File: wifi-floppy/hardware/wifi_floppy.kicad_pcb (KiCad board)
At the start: 2 copper layers, 61.4 x 54 mm, 30 parts, among them J1 Conn_02x17_Odd_Even, J2 Conn_01x04, J3 Conn_01x04, J4 Conn_01x04, Q1 BSS138, Q2 BSS138, Q3 BSS138, Q4 BSS138, Q5 BSS138, Q6 BSS138, Q7 BSS138, Q8 BSS138, U1 RaspberryPi_Pico_W, U2 74LVC541A

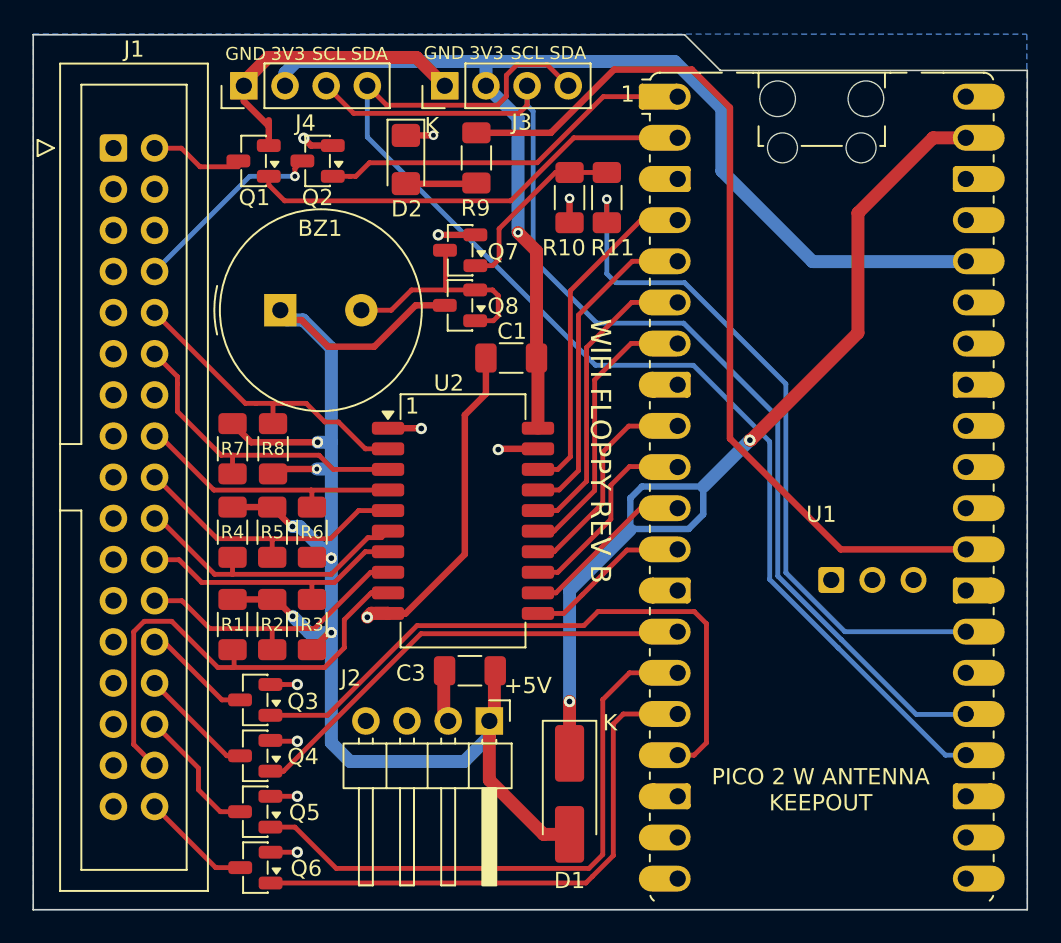
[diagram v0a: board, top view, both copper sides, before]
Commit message: Add the 22 ohms resistor for the buzzer.
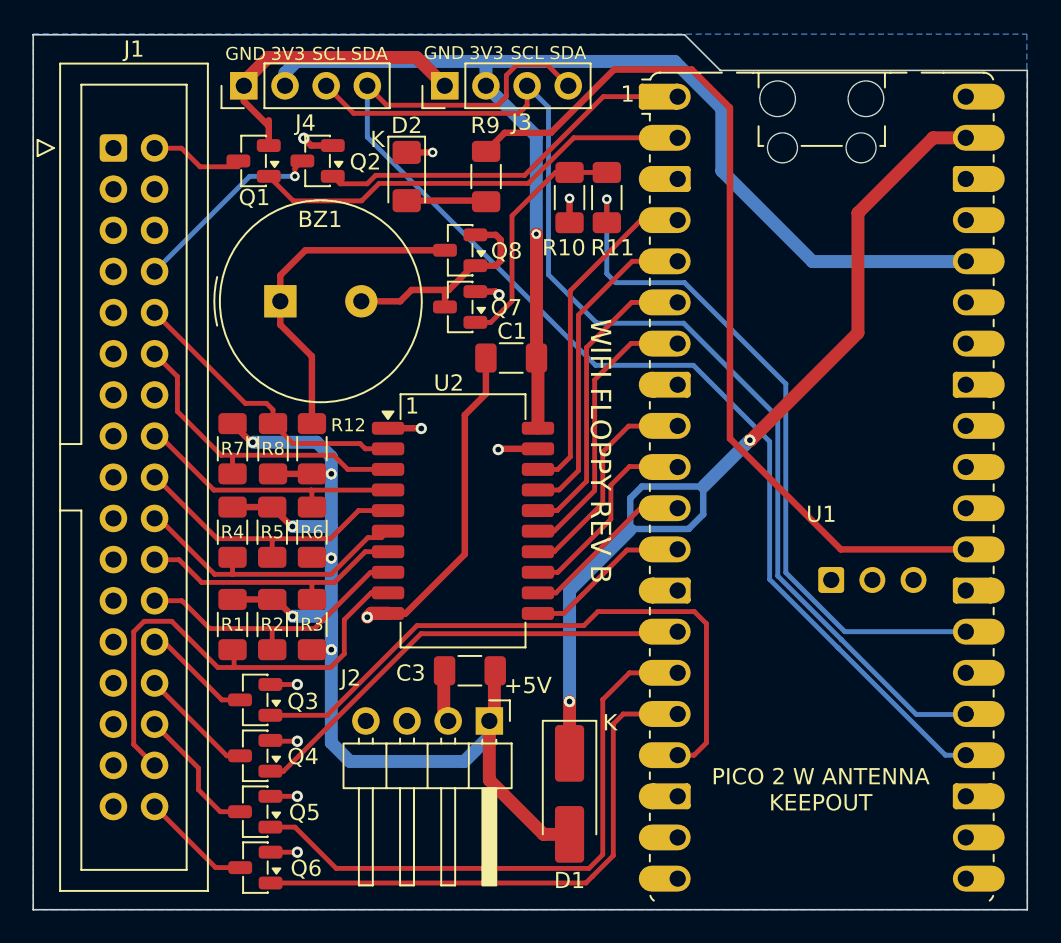
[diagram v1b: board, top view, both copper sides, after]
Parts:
- added R12: 22, wifi-floppy-lib:R_1206_3216Metric_Pad1.30x1.75mm_HandSolder, F.Cu at (118.2, 125.5)
- moved Q7 3.50 mm to (127.4, 116.8)
- moved Q8 3.40 mm to (127.4, 113.3)
- moved R9 1.30 mm to (129.0, 108.8)
- moved D2 1.05 mm to (124.1, 108.8)
- moved BZ1 0.55 mm to (116.3, 116.5)
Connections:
- BZ1 pad 1: +5V -> Net-(BZ1-+)
- Q8 pad 3: +5V -> Net-(BZ1-+)
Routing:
- net +5V: track 93.5 -> 70.9 mm
- net Net-(BZ1-+): track 0.00 -> 20.8 mm
- net Net-(Q7-G): track 11.6 -> 15.0 mm
- net GND: track 60.9 -> 60.1 mm
- net SEL0_B: track 19.1 -> 18.4 mm
- net Net-(BZ1--): track 14.4 -> 13.7 mm
- net Net-(D2-A): track 4.38 -> 4.93 mm

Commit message: Added double footprint for the buzzer (6.5 mm and 5 mm)
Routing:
- net Net-(BZ1--): track 13.7 -> 17.9 mm
- net Net-(BZ1-+): track 20.8 -> 21.9 mm
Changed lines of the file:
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@@
 			)
 		)
-		(property "LCSC" "DNP"
+		(property "LCSC" "C2687681"
 			(at 0 0 0)
 			(unlocked yes)
@@
 		)
 		(fp_line
-			(start -1.3 -1)
-			(end -1.3 1)
+			(start -1.778 -1)
+			(end -1.778 1)
 			(stroke
 				(width 0.1)
@@
 		)
 		(pad "1" thru_hole rect
-			(at 0 0)
-			(size 2 2)
+			(at -0.75 0)
+			(size 1.6 1.6)
+			(drill 0.8)
+			(layers "*.Cu" "*.Mask")
+			(remove_unused_layers no)
+			(net "Net-(BZ1-+)")
+			(pinfunction "+_1")
+			(pintype "passive")
+		)
+		(pad "1" thru_hole rect
+			(at 2.5 -2.5)
+			(size 1.6 1.6)
 			(drill 1)
 			(layers "*.Cu" "*.Mask")
@@
 		)
 		(pad "2" thru_hole circle
-			(at 5 0)
-			(size 2 2)
+			(at 2.5 2.5)
+			(size 1.6 1.6)
 			(drill 1)
 			(layers "*.Cu" "*.Mask")
@@
 			(pintype "passive")
 		)
+		(pad "2" thru_hole circle
+			(at 5.75 0)
+			(size 1.6 1.6)
+			(drill 0.8)
+			(layers "*.Cu" "*.Mask")
+			(remove_unused_layers no)
+			(net "Net-(BZ1--)")
+			(pinfunction "-_2")
+			(pintype "passive")
+		)
 		(embedded_fonts no)
 		(model "${KICAD10_3DMODEL_DIR}/Buzzer_Beeper.3dshapes/Buzzer_TDK_PS1240P02BT_D12.2mm_H6.5mm.step"
@@
 	)
 	(segment
+		(start 115.55 119.2)
+		(end 115.55 116.45)
+		(width 0.4)
+		(layer "F.Cu")
+		(net "Net-(BZ1-+)")
+	)
+	(segment
+		(start 126.3625 113.2)
+		(end 126.4625 113.3)
+		(width 0.4)
+		(layer "F.Cu")
+		(net "Net-(BZ1-+)")
+	)
+	(segment
+		(start 115.55 115.05)
+		(end 116.3 114.3)
+		(width 0.4)
+		(layer "F.Cu")
+		(net "Net-(BZ1-+)")
+	)
+	(segment
+		(start 116.3 114.3)
+		(end 116.675 113.925)
+		(width 0.4)
+		(layer "F.Cu")
+		(net "Net-(BZ1-+)")
+	)
+	(segment
+		(start 116.675 113.925)
+		(end 116.7 113.95)
+		(width 0.4)
+		(layer "F.Cu")
+		(net "Net-(BZ1-+)")
+	)
+	(segment
+		(start 118.8 113.95)
+		(end 120.45 113.95)
+		(width 0.4)
+		(layer "F.Cu")
+		(net "Net-(BZ1-+)")
+	)
+	(segment
+		(start 126.4625 113.3)
+		(end 126.5 113.3375)
+		(width 0.3)
+		(layer "F.Cu")
+		(net "Net-(BZ1-+)")
+	)
+	(segment
+		(start 116.525 120.175)
+		(end 118.25 121.9)
+		(width 0.4)
+		(layer "F.Cu")
+		(net "Net-(BZ1-+)")
+	)
+	(segment
+		(start 115.55 116.45)
+		(end 115.55 115.05)
+		(width 0.4)
+		(layer "F.Cu")
+		(net "Net-(BZ1-+)")
+	)
+	(segment
+		(start 121.2 113.2)
+		(end 126.3625 113.2)
+		(width 0.4)
+		(layer "F.Cu")
+		(net "Net-(BZ1-+)")
+	)
+	(segment
+		(start 116.525 120.175)
+		(end 115.55 119.2)
+		(width 0.4)
+		(layer "F.Cu")
+		(net "Net-(BZ1-+)")
+	)
+	(segment
+		(start 116.7 113.95)
+		(end 118.8 113.95)
+		(width 0.4)
+		(layer "F.Cu")
+		(net "Net-(BZ1-+)")
+	)
+	(segment
+		(start 118.25 121.9)
+		(end 118.25 124)
+		(width 0.4)
+		(layer "F.Cu")
+		(net "Net-(BZ1-+)")
+	)
+	(segment
+		(start 120.45 113.95)
+		(end 121.2 113.2)
+		(width 0.4)
+		(layer "F.Cu")
+		(net "Net-(BZ1-+)")
+	)
+	(segment
 		(start 128.3375 114.25)
 		(end 129.6 114.25)
@@
 	)
 	(segment
-		(start 121.3 116.45)
-		(end 123.7 116.45)
+		(start 122.05 116.45)
+		(end 122.05 117.6)
 		(width 0.4)
 		(layer "F.Cu")
@@
 	)
 	(segment
-		(start 129.9 113.95)
-		(end 129.9 112.65)
+		(start 120.7 118.95)
+		(end 118.8 118.95)
 		(width 0.4)
 		(layer "F.Cu")
@@
 	)
 	(segment
-		(start 123.7 116.45)
-		(end 124.4 115.75)
+		(start 124.4 115.75)
+		(end 126.45 115.75)
+		(width 0.4)
+		(layer "F.Cu")
+		(net "Net-(BZ1--)")
+	)
+	(segment
+		(start 129.9 113.95)
+		(end 129.9 112.65)
 		(width 0.4)
 		(layer "F.Cu")
@@
 	)
 	(segment
-		(start 124.4 115.75)
-		(end 126.45 115.75)
+		(start 126.45 115.75)
+		(end 126.4625 115.7625)
 		(width 0.4)
 		(layer "F.Cu")
@@
 	)
 	(segment
-		(start 126.45 115.75)
-		(end 126.4625 115.7625)
+		(start 123.7 116.45)
+		(end 124.4 115.75)
 		(width 0.4)
 		(layer "F.Cu")
@@
 	)
 	(segment
+		(start 122.05 117.6)
+		(end 120.7 118.95)
+		(width 0.4)
+		(layer "F.Cu")
+		(net "Net-(BZ1--)")
+	)
+	(segment
+		(start 122.05 116.45)
+		(end 123.7 116.45)
+		(width 0.4)
+		(layer "F.Cu")
+		(net "Net-(BZ1--)")
+	)
+	(segment
 		(start 115.6875 148.9)
 		(end 117.2 148.9)
@@
 		(net "CHNG_B")
 	)
-	(segment
-		(start 116.3 114.85)
-		(end 117.85 113.3)
-		(width 0.4)
-		(layer "F.Cu")
-		(net "Net-(BZ1-+)")
-	)
-	(segment
-		(start 118.25 119.85)
-		(end 118.25 124)
-		(width 0.4)
-		(layer "F.Cu")
-		(net "Net-(BZ1-+)")
-	)
-	(segment
-		(start 117.85 113.3)
-		(end 126.4625 113.3)
-		(width 0.4)
-		(layer "F.Cu")
-		(net "Net-(BZ1-+)")
-	)
-	(segment
-		(start 116.3 116.45)
-		(end 116.3 114.85)
-		(width 0.4)
-		(layer "F.Cu")
-		(net "Net-(BZ1-+)")
-	)
-	(segment
-		(start 116.3 117.9)
-		(end 118.25 119.85)
-		(width 0.4)
-		(layer "F.Cu")
-		(net "Net-(BZ1-+)")
-	)
-	(segment
-		(start 126.4625 113.3)
-		(end 126.5 113.3375)
-		(width 0.3)
-		(layer "F.Cu")
-		(net "Net-(BZ1-+)")
-	)
-	(segment
-		(start 116.3 116.45)
-		(end 116.3 117.9)
-		(width 0.4)
-		(layer "F.Cu")
-		(net "Net-(BZ1-+)")
-	)
 	(zone
